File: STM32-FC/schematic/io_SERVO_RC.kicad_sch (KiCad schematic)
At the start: 10 parts, among them J5 PWM_Conn_3x04, J6 PWM_Conn_3x04, J7 PWM_Conn_3x04, J8 ZH 1.5mm 4P, J9 GH 1.25mm 4P, Q2 S9013

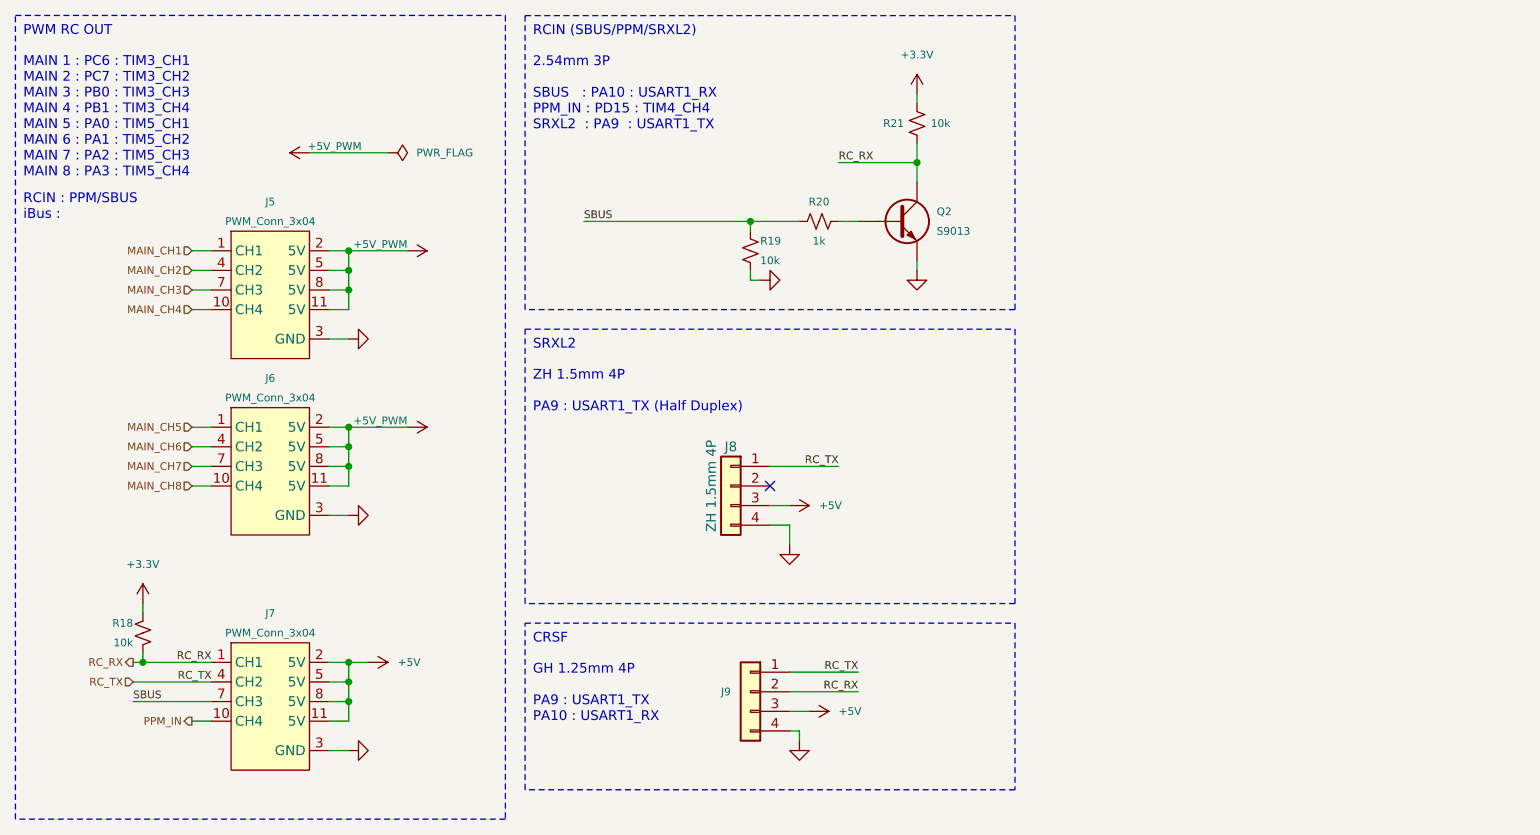
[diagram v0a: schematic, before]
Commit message: add: servo power & comment
- Servo power diode add
- comment update
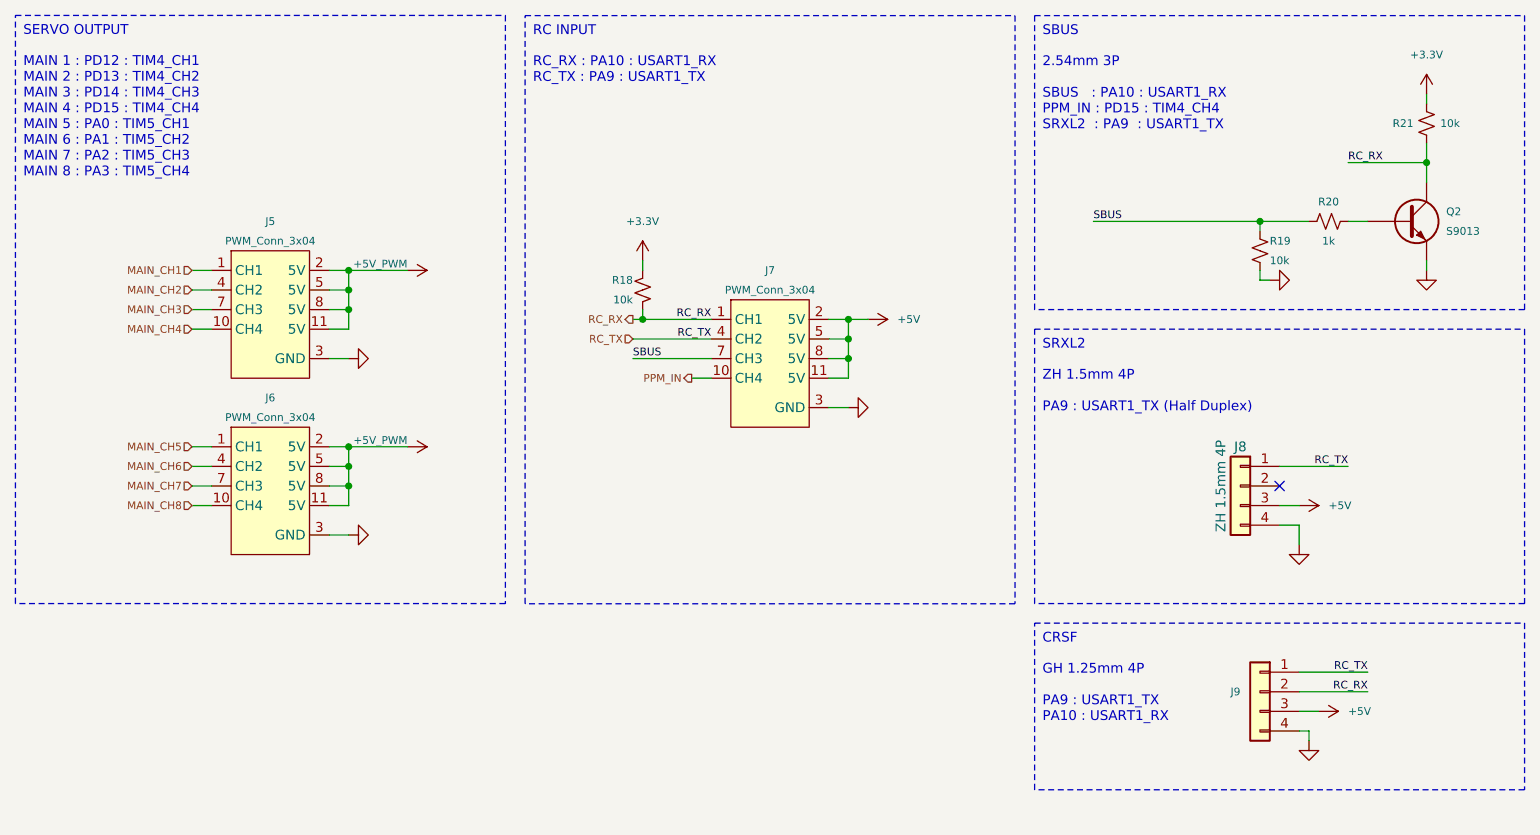
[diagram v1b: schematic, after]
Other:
- note added: "MAIN 1 : PD12 : TIM4_CH1 MAIN 2 : PD13 : TIM4_CH2 MAIN 3 : PD14 : TIM4_CH3 MAIN 4 : PD15 : TIM4_CH4 MAIN 5 : PA0 : TIM5_CH1 MAIN 6 : PA1 : TIM5_CH2 MAIN 7 : PA2 : TIM5_CH3 MAIN 8 : PA3 : TIM5_CH4"
- note added: "RC INPUT"
- note added: "RC_RX : PA10 : USART1_RX RC_TX : PA9 : USART1_TX"
- note added: "SBUS"
- note added: "SERVO OUTPUT"
- note removed: "MAIN 1 : PC6 : TIM3_CH1 MAIN 2 : PC7 : TIM3_CH2 MAIN 3 : PB0 : TIM3_CH3 MAIN 4 : PB1 : TIM3_CH4 MAIN 5 : PA0 : TIM5_CH1 MAIN 6 : PA1 : TIM5_CH2 MAIN 7 : PA2 : TIM5_CH3 MAIN 8 : PA3 : TIM5_CH4"
- note removed: "PWM RC OUT"
- note removed: "RCIN (SBUS/PPM/SRXL2)"
- note removed: "RCIN : PPM/SBUS iBus :"
- moved on the sheet: J5, J6, J7, J8, J9, Q2, R18, R19, R20, R21

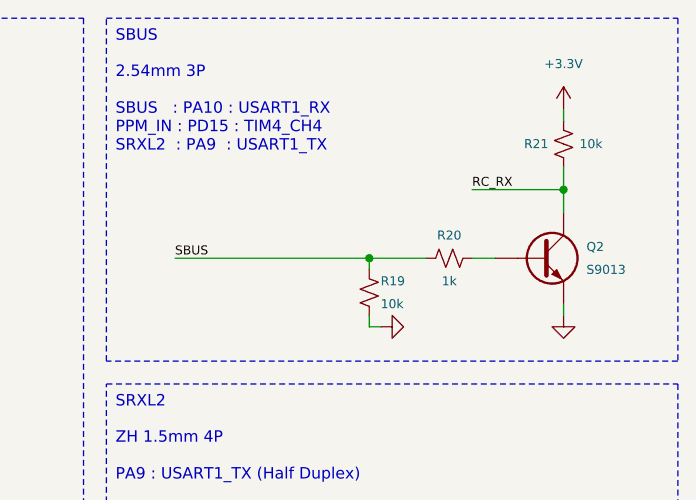
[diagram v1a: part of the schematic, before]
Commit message: update : BJT to MOSFET
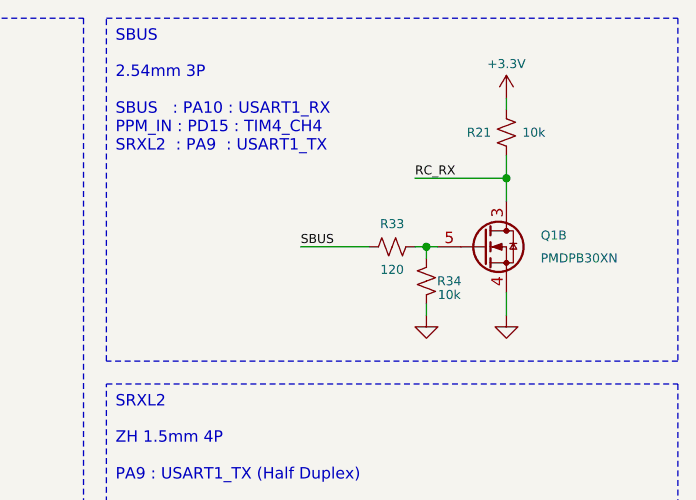
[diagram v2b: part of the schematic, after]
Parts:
- removed Q2: S9013, Package_TO_SOT_SMD:SOT-23-3, symbol Device:Q_NPN
- removed R19: 10k, Resistor_SMD:R_0402_1005Metric, symbol Device:R_Small_US
- added Q1: PMDPB30XN, Nexperia_PMD:Nexperia_SOT1118, symbol Nexperia_PMD:PMDPB30XN
- added R34: 10k, Resistor_SMD:R_0402_1005Metric, symbol Device:R_Small_US
- J5, J6, J7: footprint PWM_Connector:PWM_Conn_3x04 -> PWM_Connector:PWM_Conn_3x04_JLC; LCSC C32713291 -> C3327492
- R33: renamed from R20; value 1k -> 120; LCSC C11702 -> C25079
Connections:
- net GND: now also Q1.4 (S), R34.2
- net RC_RX: now also Q1.3 (D), Q1.8 (D)
- net at R33.2: now also Q1.5 (G), R34.1
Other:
- moved on the sheet: R21, R33

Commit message: WIP : pcb part layout &* BOM udpate
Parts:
- J5, J6, J7: LCSC C3327492 -> C3325573
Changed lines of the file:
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@@
 			)
 		)
-		(property "LCSC" "C3327492"
+		(property "LCSC" "C3325573"
 			(at 120.65 58.42 0)
 			(effects
@@
 			)
 		)
-		(property "LCSC" "C3327492"
+		(property "LCSC" "C3325573"
 			(at 55.88 52.07 0)
 			(effects
@@
 			)
 		)
-		(property "LCSC" "C3327492"
+		(property "LCSC" "C3325573"
 			(at 55.88 74.93 0)
 			(effects

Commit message: update : AHRS PCB layout & routing done
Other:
- note added: "* for Spektrum serial receiver ** Half Duplex ZH 1.5mm 4P PA9 : USART1_TX"
- note removed: "ZH 1.5mm 4P PA9 : USART1_TX (Half Duplex)"
- moved on the sheet: J8, J9
